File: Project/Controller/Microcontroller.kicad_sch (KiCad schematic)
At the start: 38 parts, among them J2 SWD, J3 USB_C_Receptacle_USB2.0_16P, SW1 SW_SPDT, SW2 SW_SPDT, SW3 SW_Push, U4 STM32F446RCTx, U5 24AA64-OT, U6 USBLC6-2SC6, Y1 25 MHz

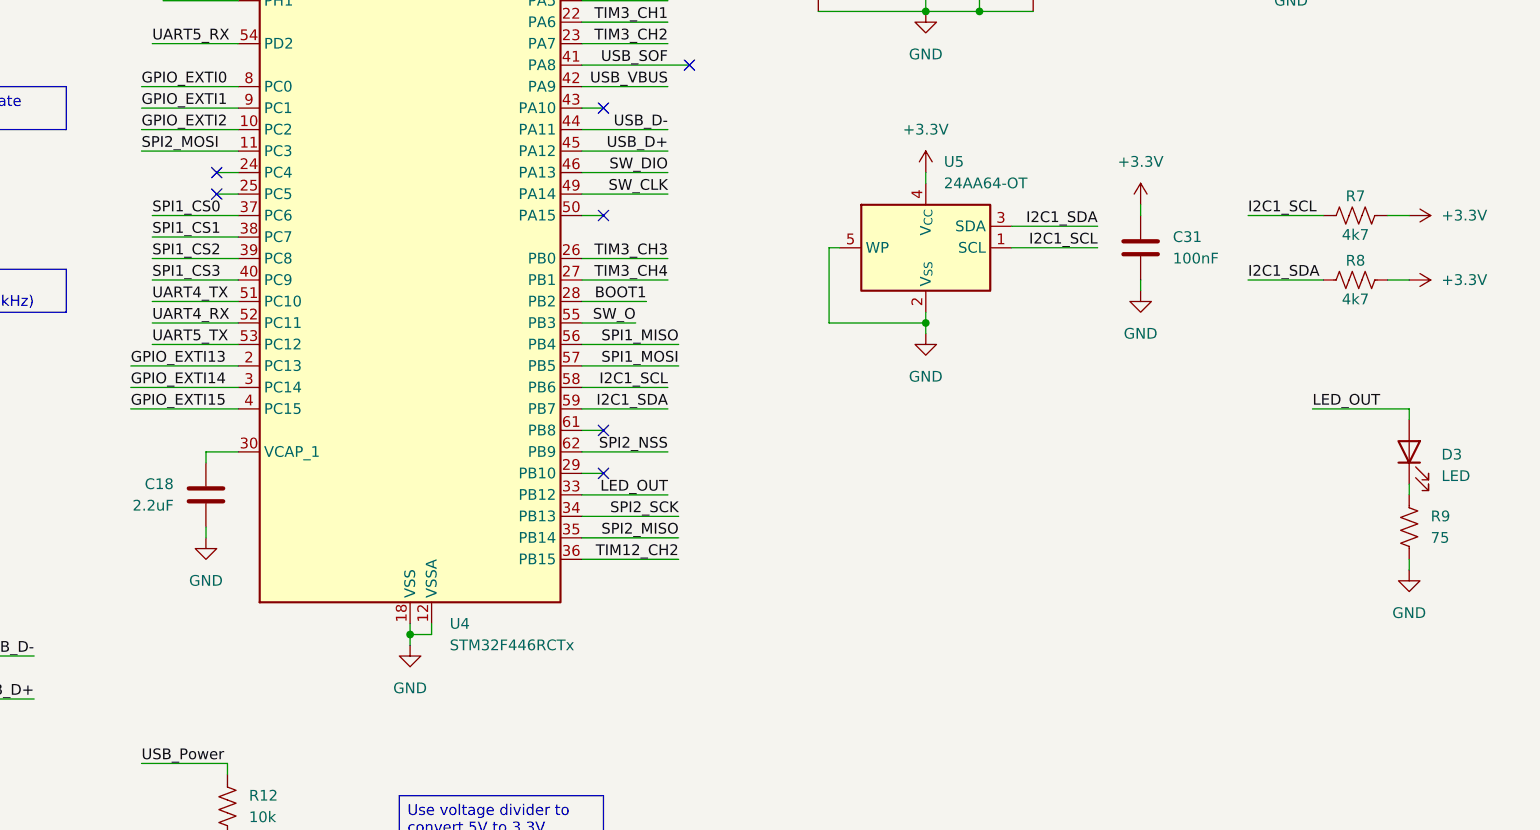
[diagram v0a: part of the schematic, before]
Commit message: Add two more LEDs and increase LED series resistance
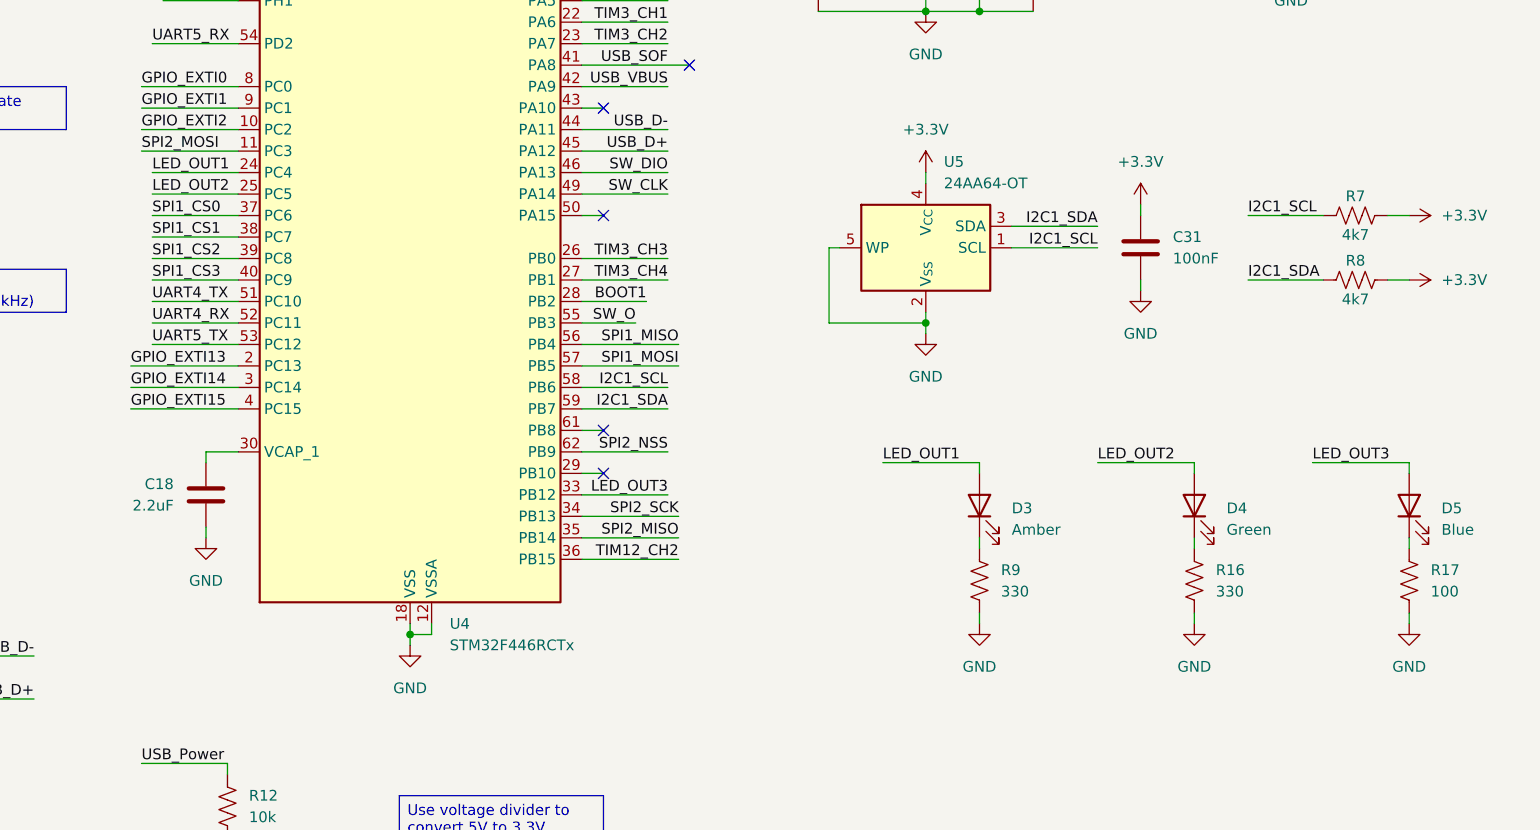
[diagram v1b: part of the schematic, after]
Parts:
- added D4: Green, LED_SMD:LED_0603_1608Metric, symbol Device:LED
- added D5: Blue, LED_SMD:LED_0603_1608Metric, symbol Device:LED
- added R16: 330, Resistor_SMD:R_0402_1005Metric, symbol Device:R_US
- added R17: 100, Resistor_SMD:R_0402_1005Metric, symbol Device:R_US
- D3: value LED -> Amber; Listing https://www.digikey.com/en/products/detail/liteon/LTST-C190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 -> https://www.digikey.com/en/products/detail/w%C3%BCrth-elekt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
- R9: value 75 -> 330; Listing https://www.digikey.com/en/products/detail/yageo/RC0402JR-0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 -> https://www.digikey.com/en/products/detail/yageo/RC0402FR-0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
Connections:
- net GND: now also R16.2, R17.2
- net LED_OUT1: now reaches U4.24 (PC4)
- net LED_OUT1: now also D3.2 (A)
- net LED_OUT2: now reaches U4.25 (PC5)
- net LED_OUT2: now also D4.2 (A)
- net LED_OUT renamed LED_OUT3
- net LED_OUT3: now also D5.2 (A); no longer D3.2 (A)
- new net: D4.1 (K), R16.1
- new net: D5.1 (K), R17.1
- no-connect marks 10 -> 8
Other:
- moved on the sheet: D3, R9

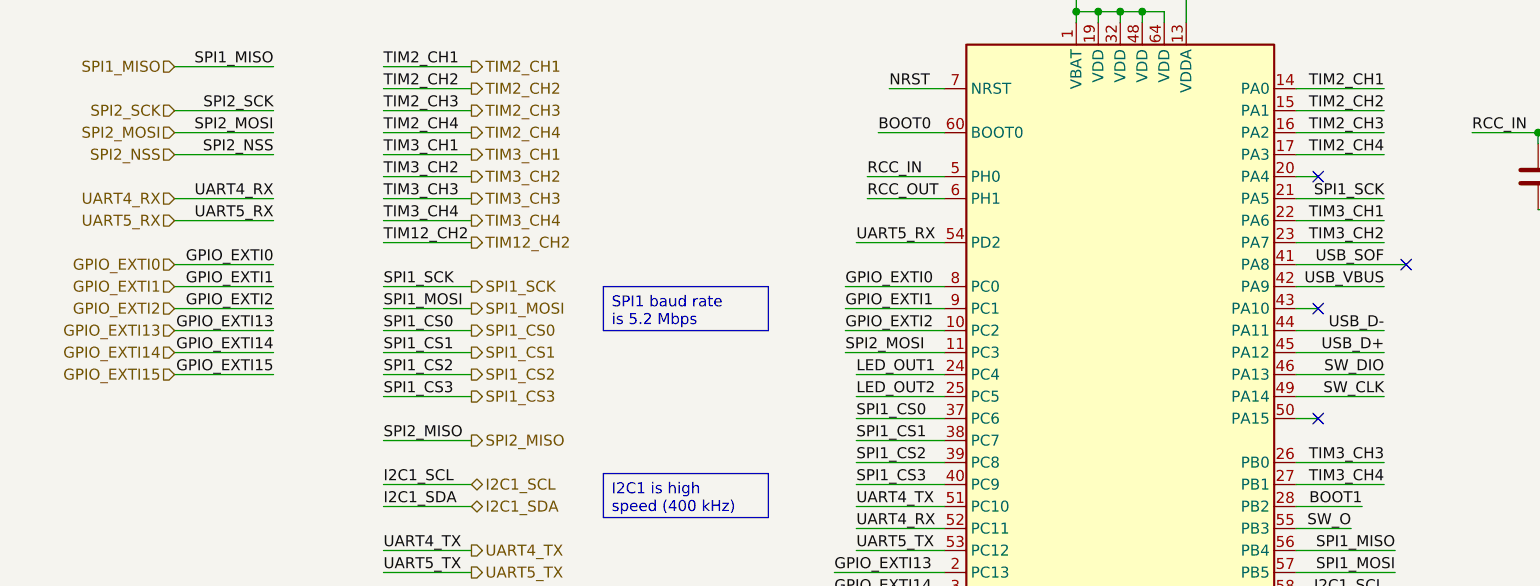
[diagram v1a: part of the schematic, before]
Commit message: Add MCP9700A temperature sensor
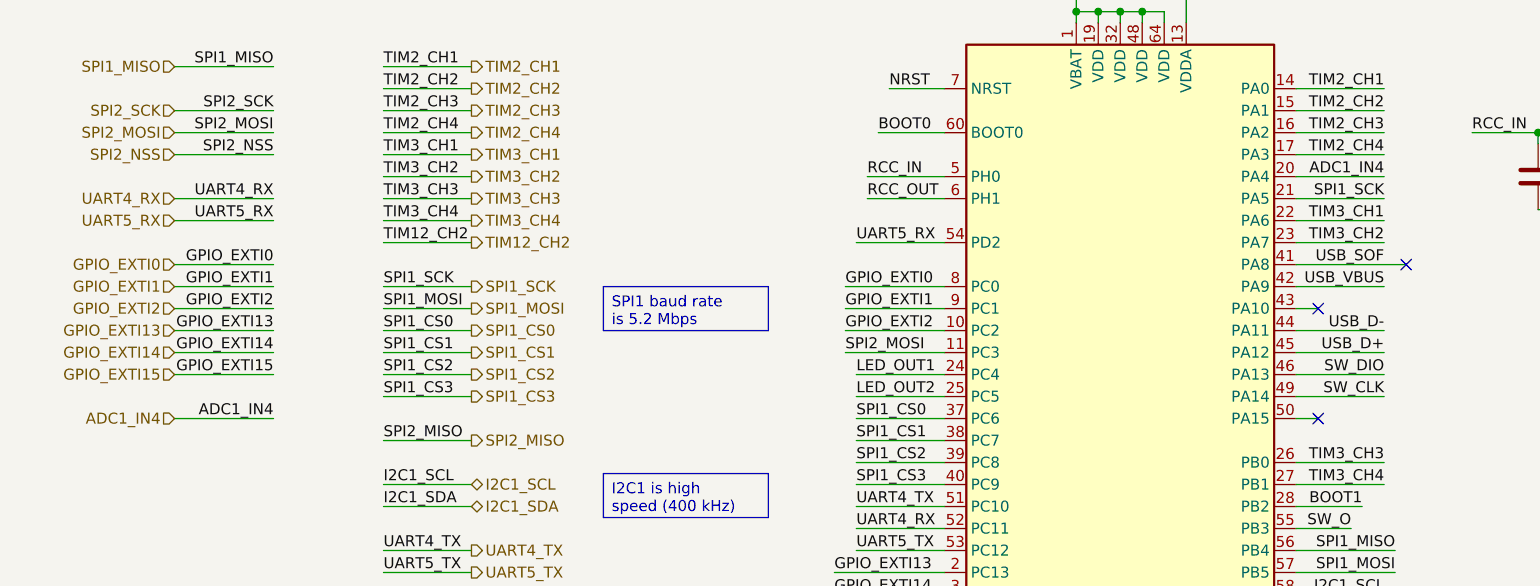
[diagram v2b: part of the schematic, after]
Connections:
- net ADC1_IN4: now reaches U4.20 (PA4)
- no-connect marks 8 -> 7
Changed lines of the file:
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@@
 	(title_block
 		(title "Microcontroller - STM32F446RCTx")
-		(date "2026-02-09")
+		(date "2026-02-10")
 		(rev "B")
 		(company "CU Boulder Senior Design Team 29 - Xu Lab")
@@
 	)
 	(no_connect
-		(at 171.45 76.2)
-	)
-	(no_connect
 		(at 55.88 170.18)
 	)
@@
 	(wire
 		(pts
-			(xy 168.91 76.2) (xy 171.45 76.2)
+			(xy 168.91 76.2) (xy 179.07 76.2)
 		)
 		(stroke
@@
 	(wire
 		(pts
+			(xy 39.37 104.14) (xy 50.8 104.14)
+		)
+		(stroke
+			(width 0)
+			(type default)
+		)
+	)
+	(wire
+		(pts
 			(xy 54.61 154.94) (xy 53.34 154.94)
 		)
@@
 		)
 	)
+	(label "ADC1_IN4"
+		(at 179.07 76.2 180)
+		(effects
+			(font
+				(size 1.27 1.27)
+			)
+			(justify right bottom)
+		)
+	)
 	(label "SPI1_MISO"
 		(at 180.34 119.38 180)
@@
 		)
 	)
+	(label "ADC1_IN4"
+		(at 50.8 104.14 180)
+		(effects
+			(font
+				(size 1.27 1.27)
+			)
+			(justify right bottom)
+		)
+	)
 	(label "GPIO_EXTI15"
 		(at 50.8 99.06 180)
@@
 		)
 	)
+	(hierarchical_label "ADC1_IN4"
+		(shape input)
+		(at 39.37 104.14 180)
+		(effects
+			(font
+				(size 1.27 1.27)
+			)
+			(justify right)
+		)
+	)

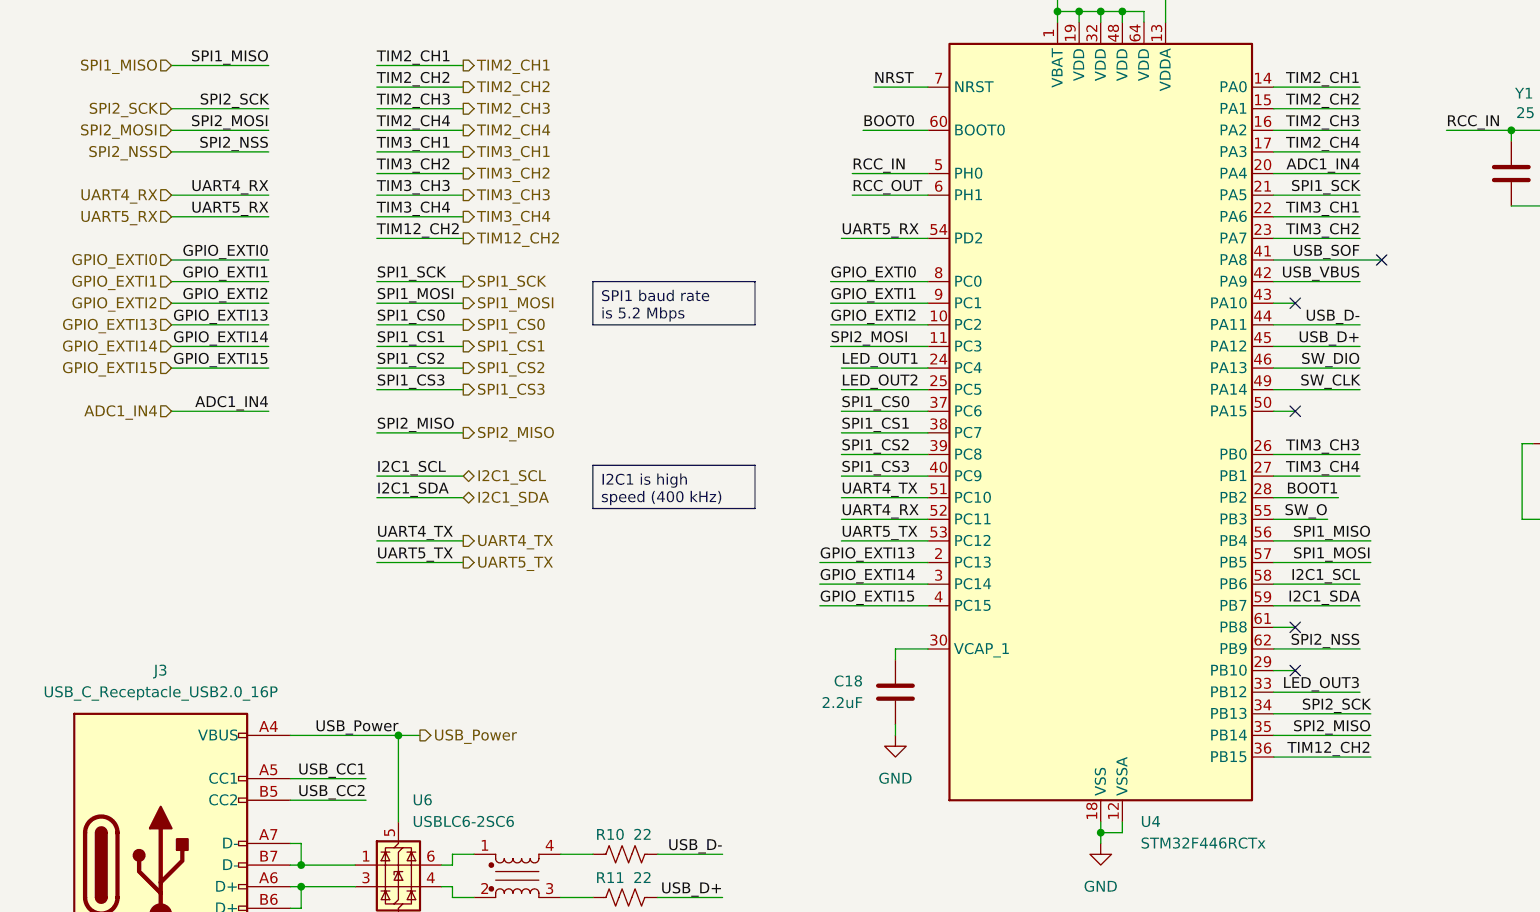
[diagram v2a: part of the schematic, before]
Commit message: Reorganize pin layout
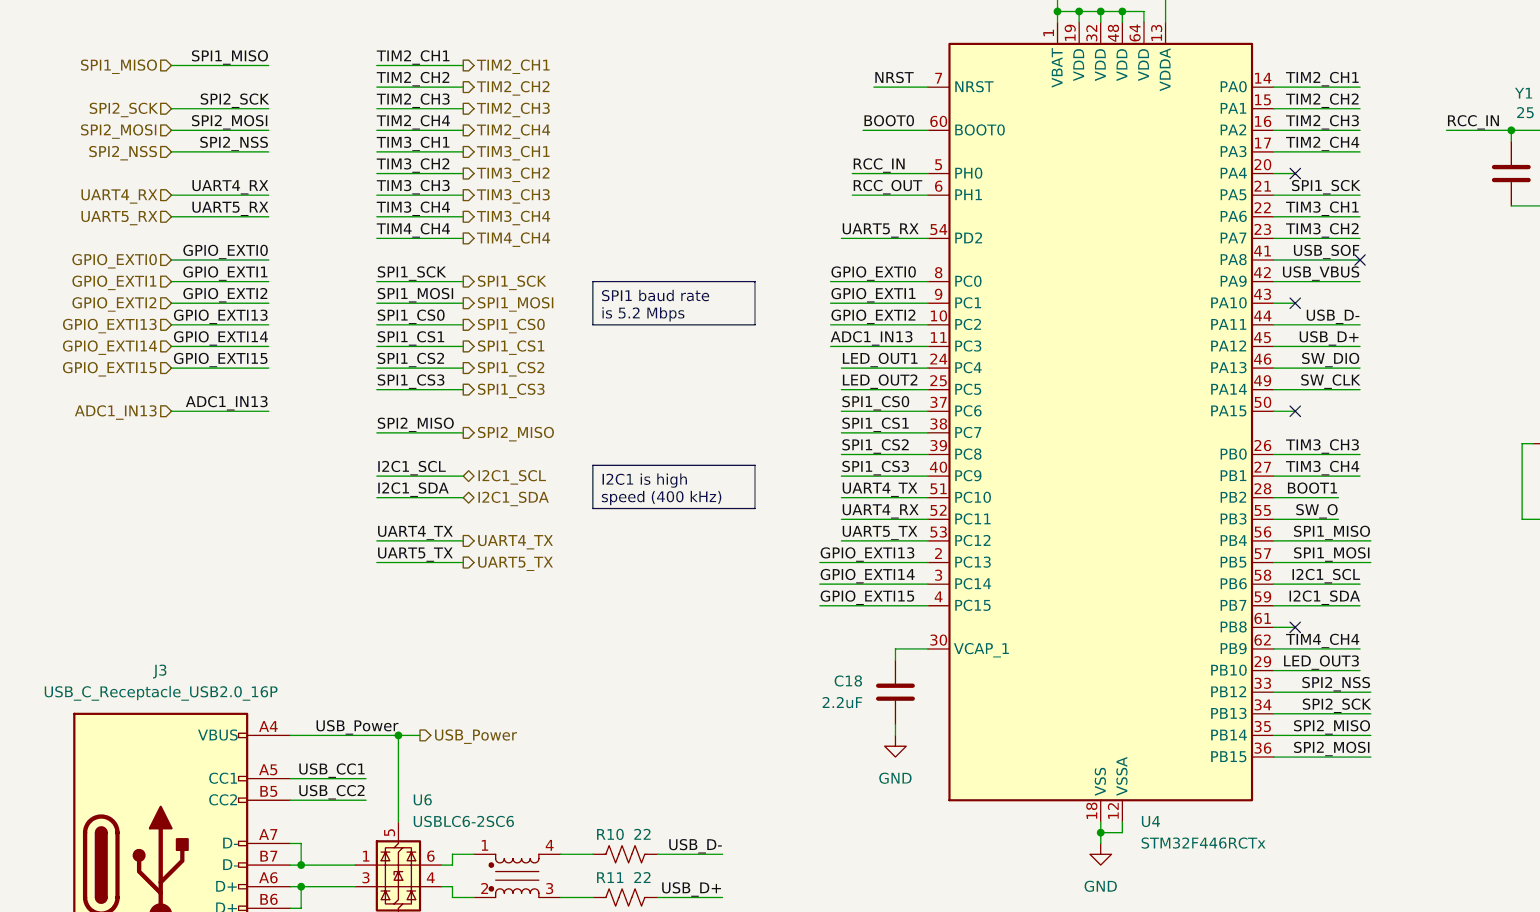
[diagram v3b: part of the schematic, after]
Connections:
- net TIM12_CH2 is gone; now on net SPI2_MOSI: U4.36 (PB15)
- net LED_OUT3: now also U4.29 (PB10); no longer U4.33 (PB12)
- net SPI2_MOSI: no longer U4.11 (PC3)
- net SPI2_NSS: now also U4.33 (PB12); no longer U4.62 (PB9)
- net ADC1_IN4: no longer names the net of U4.20 (PA4)
- new net ADC1_IN13: U4.11 (PC3)
- new net TIM4_CH4: U4.62 (PB9)
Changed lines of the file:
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@@
 	(title_block
 		(title "Microcontroller - STM32F446RCTx")
-		(date "2026-02-10")
+		(date "2026-02-11")
 		(rev "B")
 		(company "CU Boulder Senior Design Team 29 - Xu Lab")
@@
 	)
 	(no_connect
-		(at 171.45 134.62)
+		(at 171.45 76.2)
 	)
 	(no_connect
-		(at 181.61 86.36)
+		(at 179.07 86.36)
 	)
 	(no_connect
@@
 	(wire
 		(pts
-			(xy 88.9 36.83) (xy 106.68 36.83)
+			(xy 168.91 76.2) (xy 171.45 76.2)
 		)
 		(stroke
@@
 	(wire
 		(pts
-			(xy 168.91 76.2) (xy 179.07 76.2)
+			(xy 88.9 36.83) (xy 106.68 36.83)
 		)
 		(stroke
@@
 	(wire
 		(pts
-			(xy 168.91 132.08) (xy 179.07 132.08)
-		)
-		(stroke
-			(width 0)
-			(type default)
-		)
-	)
-	(wire
-		(pts
 			(xy 168.91 104.14) (xy 171.45 104.14)
 		)
@@
 	(wire
 		(pts
+			(xy 168.91 132.08) (xy 179.07 132.08)
+		)
+		(stroke
+			(width 0)
+			(type default)
+		)
+	)
+	(wire
+		(pts
 			(xy 76.2 27.94) (xy 76.2 26.67)
 		)
@@
 	(wire
 		(pts
+			(xy 168.91 137.16) (xy 180.34 137.16)
+		)
+		(stroke
+			(width 0)
+			(type default)
+		)
+	)
+	(wire
+		(pts
 			(xy 25.4 36.83) (xy 38.1 36.83)
 		)
@@
 	(wire
 		(pts
-			(xy 168.91 116.84) (xy 175.26 116.84)
+			(xy 168.91 116.84) (xy 176.53 116.84)
 		)
 		(stroke
@@
 	(wire
 		(pts
-			(xy 168.91 134.62) (xy 171.45 134.62)
+			(xy 168.91 134.62) (xy 179.07 134.62)
 		)
 		(stroke
@@
 	(wire
 		(pts
-			(xy 168.91 137.16) (xy 179.07 137.16)
-		)
-		(stroke
-			(width 0)
-			(type default)
-		)
-	)
-	(wire
-		(pts
 			(xy 209.55 118.11) (xy 209.55 116.84)
 		)
@@
 	(wire
 		(pts
+			(xy 168.91 73.66) (xy 179.07 73.66)
+		)
+		(stroke
+			(width 0)
+			(type default)
+		)
+	)
+	(wire
+		(pts
 			(xy 39.37 73.66) (xy 50.8 73.66)
 		)
@@
 	(wire
 		(pts
-			(xy 168.91 86.36) (xy 181.61 86.36)
+			(xy 168.91 86.36) (xy 179.07 86.36)
 		)
 		(stroke
@@
 	(wire
 		(pts
-			(xy 168.91 73.66) (xy 179.07 73.66)
-		)
-		(stroke
-			(width 0)
-			(type default)
-		)
-	)
-	(wire
-		(pts
 			(xy 139.7 31.75) (xy 146.05 31.75)
 		)
@@
 		)
 	)
+	(label "TIM2_CH4"
+		(at 179.07 73.66 180)
+		(effects
+			(font
+				(size 1.27 1.27)
+			)
+			(justify right bottom)
+		)
+	)
 	(label "TIM3_CH2"
 		(at 179.07 83.82 180)
@@
 		)
 	)
-	(label "TIM2_CH4"
-		(at 179.07 73.66 180)
-		(effects
-			(font
-				(size 1.27 1.27)
-			)
-			(justify right bottom)
-		)
-	)
 	(label "RCC_OUT"
 		(at 240.03 71.12 180)
@@
 		)
 	)
-	(label "ADC1_IN4"
-		(at 179.07 76.2 180)
+	(label "SPI1_MISO"
+		(at 180.34 119.38 180)
 		(effects
 			(font
@@
 		)
 	)
-	(label "SPI1_MISO"
-		(at 180.34 119.38 180)
+	(label "SW_CLK"
+		(at 274.32 69.85 180)
 		(effects
 			(font
@@
 		)
 	)
-	(label "SW_CLK"
-		(at 274.32 69.85 180)
+	(label "SPI2_NSS"
+		(at 180.34 137.16 180)
 		(effects
 			(font
@@
 		)
 	)
-	(label "SPI2_MOSI"
+	(label "ADC1_IN13"
 		(at 116.84 96.52 0)
 		(effects
@@
 	)
 	(label "LED_OUT3"
-		(at 179.07 137.16 180)
+		(at 179.07 134.62 180)
 		(effects
 			(font
@@
 		)
 	)
-	(label "SPI2_NSS"
-		(at 179.07 132.08 180)
-		(effects
-			(font
-				(size 1.27 1.27)
-			)
-			(justify right bottom)
-		)
-	)
 	(label "SPI1_CS2"
 		(at 118.11 109.22 0)
@@
 	)
 	(label "SW_O"
-		(at 175.26 116.84 180)
+		(at 176.53 116.84 180)
 		(effects
 			(font
@@
 		)
 	)
+	(label "TIM4_CH4"
+		(at 179.07 132.08 180)
+		(effects
+			(font
+				(size 1.27 1.27)
+			)
+			(justify right bottom)
+		)
+	)
 	(label "GPIO_EXTI2"
 		(at 116.84 93.98 0)
@@
 		)
 	)
-	(label "ADC1_IN4"
+	(label "ADC1_IN13"
 		(at 50.8 104.14 180)
 		(effects
@@
 		)
 	)
-	(label "TIM12_CH2"
+	(label "TIM4_CH4"
 		(at 63.5 83.82 0)
 		(effects
@@
 		)
 	)
-	(label "TIM12_CH2"
+	(label "SPI2_MOSI"
 		(at 180.34 144.78 180)
 		(effects
@@
 		)
 	)
-	(hierarchical_label "ADC1_IN4"
+	(hierarchical_label "ADC1_IN13"
 		(shape input)
 		(at 39.37 104.14 180)
@@
 		)
 	)
-	(hierarchical_label "TIM12_CH2"
+	(hierarchical_label "TIM4_CH4"
 		(shape output)
 		(at 73.66 83.82 0)
